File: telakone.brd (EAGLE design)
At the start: 160 x 100 mm, 27 parts, among them X2 MPT0.5/8-2.54

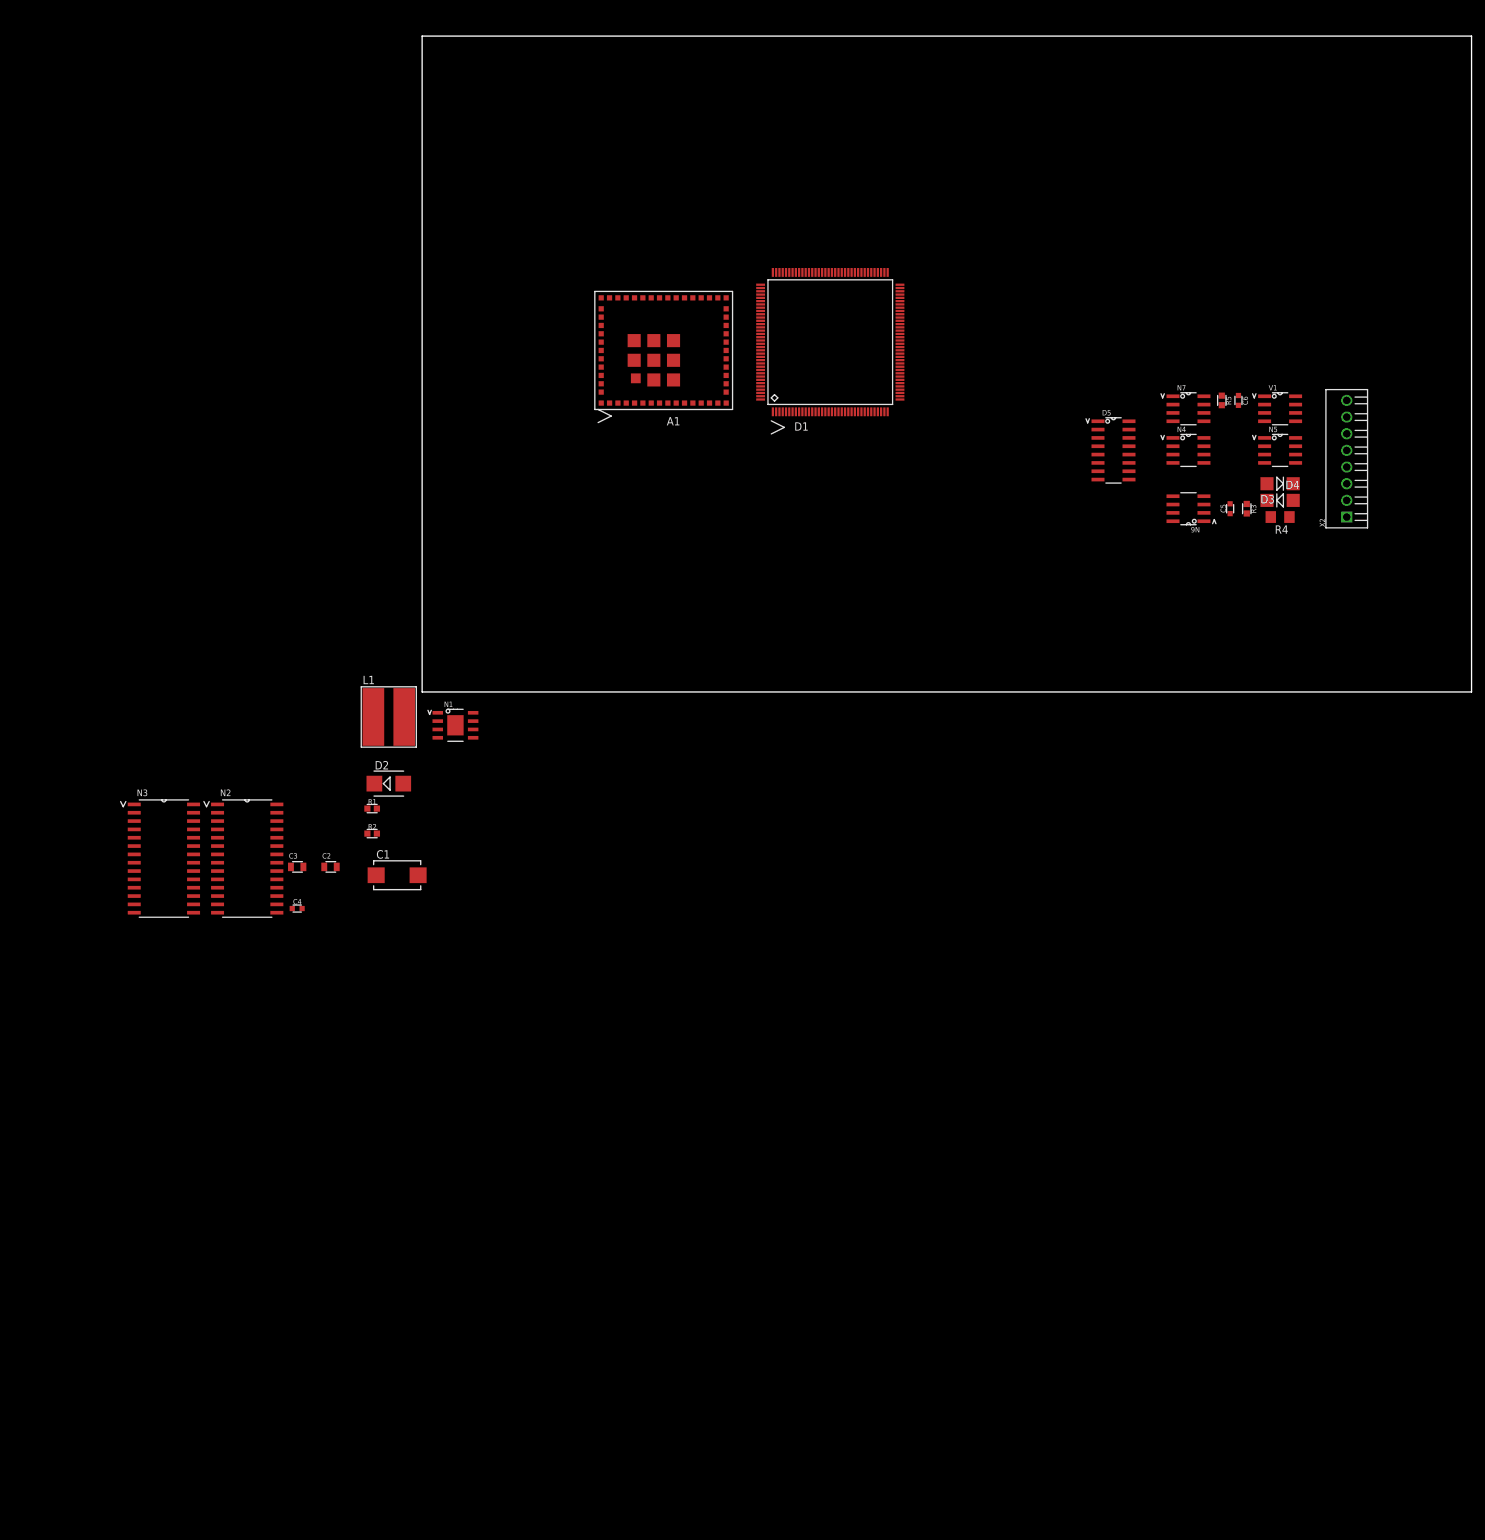
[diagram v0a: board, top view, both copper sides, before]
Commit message: p-fet outputs
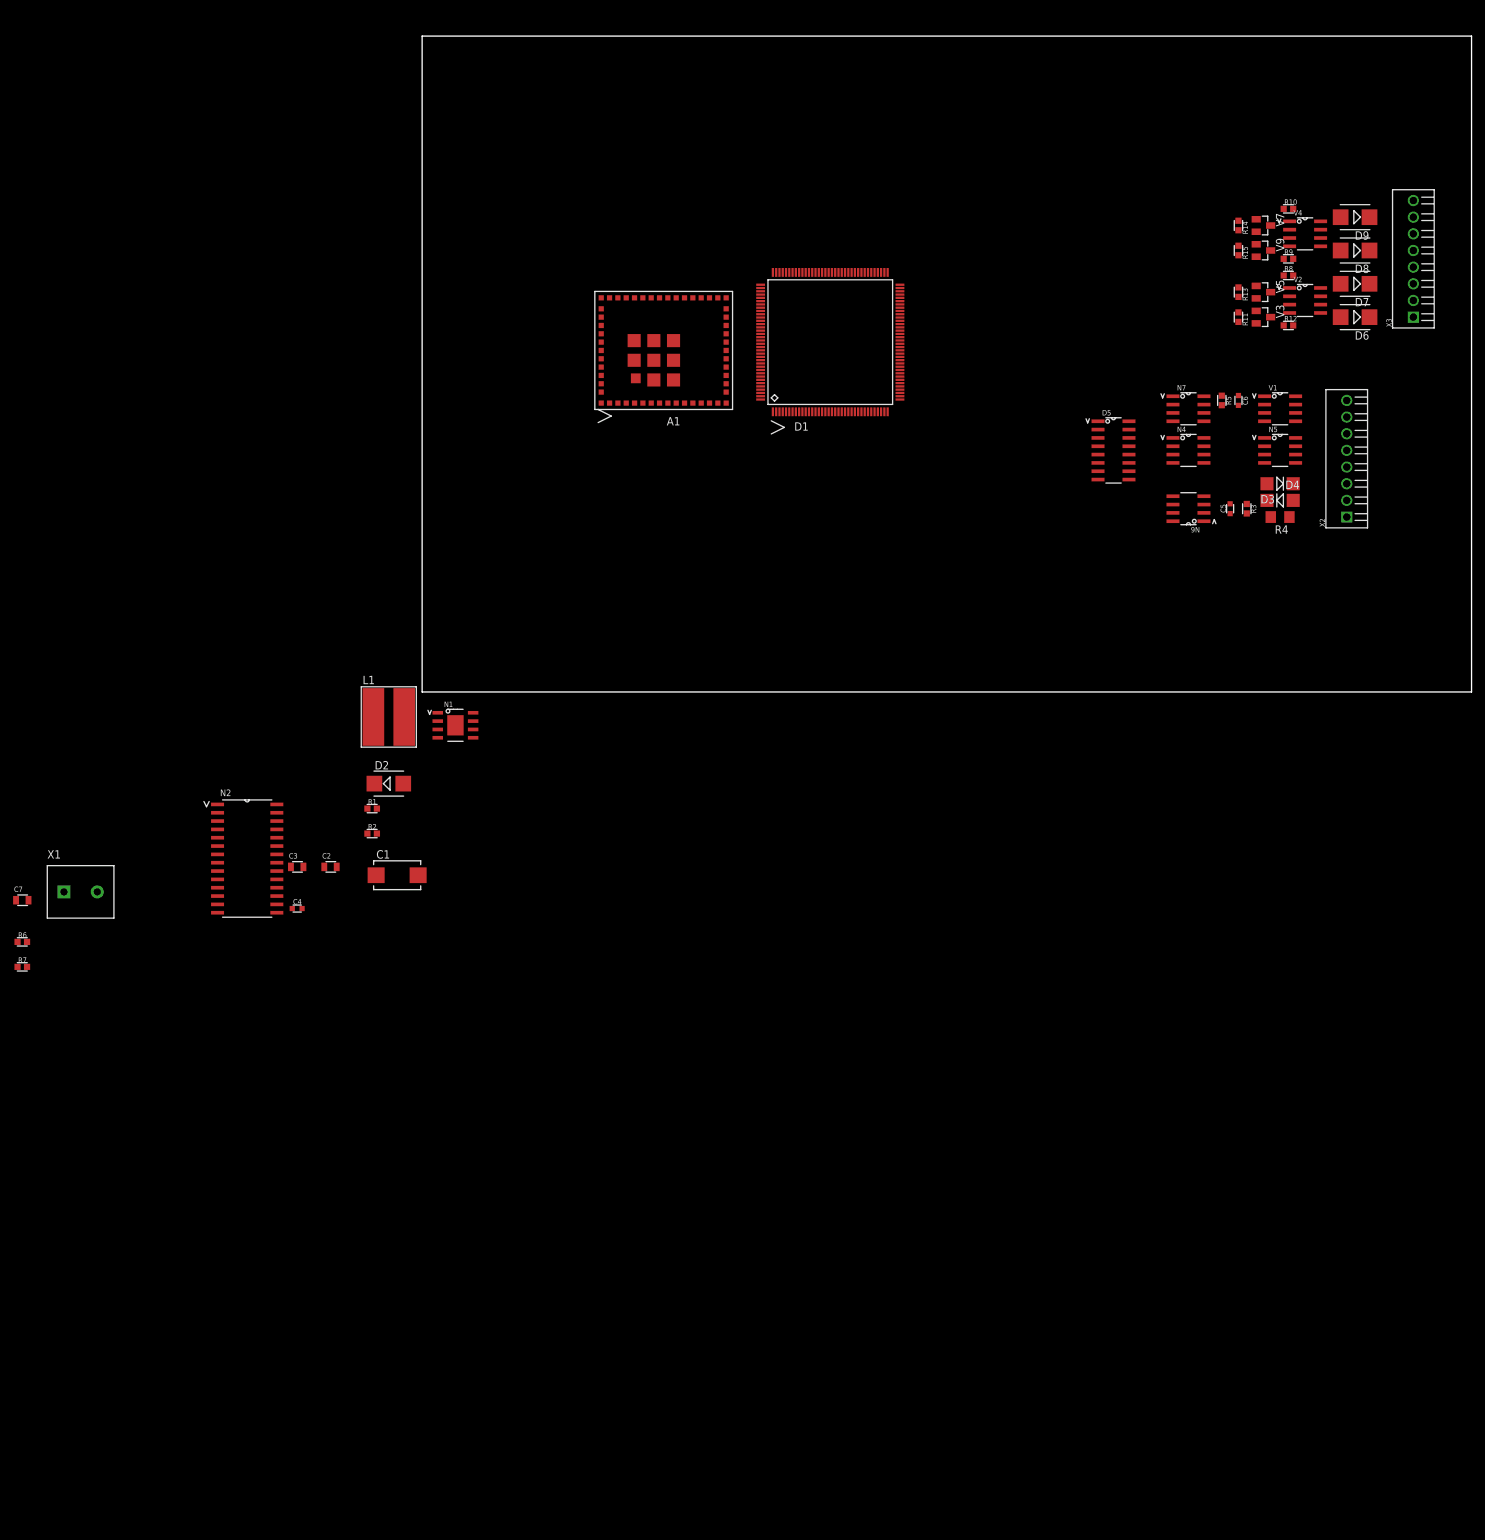
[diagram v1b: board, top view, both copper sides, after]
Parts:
- removed N3: BTM7710G, omat_ic_2:SOIC28-W_MC
- added C7: (no value), omat_ic_2:C0805
- added D6, D7, D8, D9: SK34B, diode:SMB
- added R10, R11, R12, R13, R14, R15, R6, R7, R8, R9: (no value), omat_ic_2:R0603
- added V2, V4: AO4803A, omat_ic_2:SOIC8-N_MC
- added V3, V5, V7, V9: 2N7002K, omat_ic_2:SOT23
- added X1: (no value), omat_ic_2:TE_RUUVILIITIN2
- added X3: MPT0.5/8-2.54, omat_ic_2:MPT0.5/8-2.54
- D2: value STPS340U -> SK34B
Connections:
- new net +12V: C2.1, C3.1, C7.1, N1.7, N2.10, N2.19, N2.24, N2.5, R10.2, R12.2, R8.2, R9.2, V2.1, V2.3, V4.1, V4.3
- new net N$10: R8.1, V2.2, V5.3
- new net N$11: R12.1, V2.4, V3.3
- new net N$12: R13.1, V5.1
- new net N$13: R9.1, V4.4, V7.3
- new net N$14: R14.1, V7.1
- new net N$15: R10.1, V4.2, V9.3
- new net N$16: R15.1, V9.1
- new net N$17: D9.C, X3.7
- new net N$19: D8.C, X3.5
- new net N$20: D7.C, X3.3
- new net N$21: D6.C, X3.1
- new net N$3: N2.12, N2.14, N2.15, N2.18, N2.20, N2.21, X1.1
- new net N$5: N2.1, N2.22, N2.23, N2.25, N2.28, N2.3, X1.2
- new net N$7: N2.8
- new net N$8: N2.13, N2.7, R7.2
- new net N$9: N2.2, N2.9, R6.2
- new net NERT: D6.A, V2.5, V2.6
- new net NERT1: D7.A, V2.7, V2.8
- new net NERT2: D8.A, V4.5, V4.6
- new net NERT3: D9.A, V4.7, V4.8
- net GND: now also C7.2, N2.16, N2.17, N2.26, N2.27, N2.6, R11.2, R13.2, R14.2, R15.2, R6.1, R7.1, V3.2, V5.2, V7.2, V9.2, X3.2, X3.4, X3.6, X3.8
- net N$6: now also R11.1, V3.1; no longer C2.1, C3.1, N1.7

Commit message: placement sketching, temp and acceleration sensors, 2nd drive group
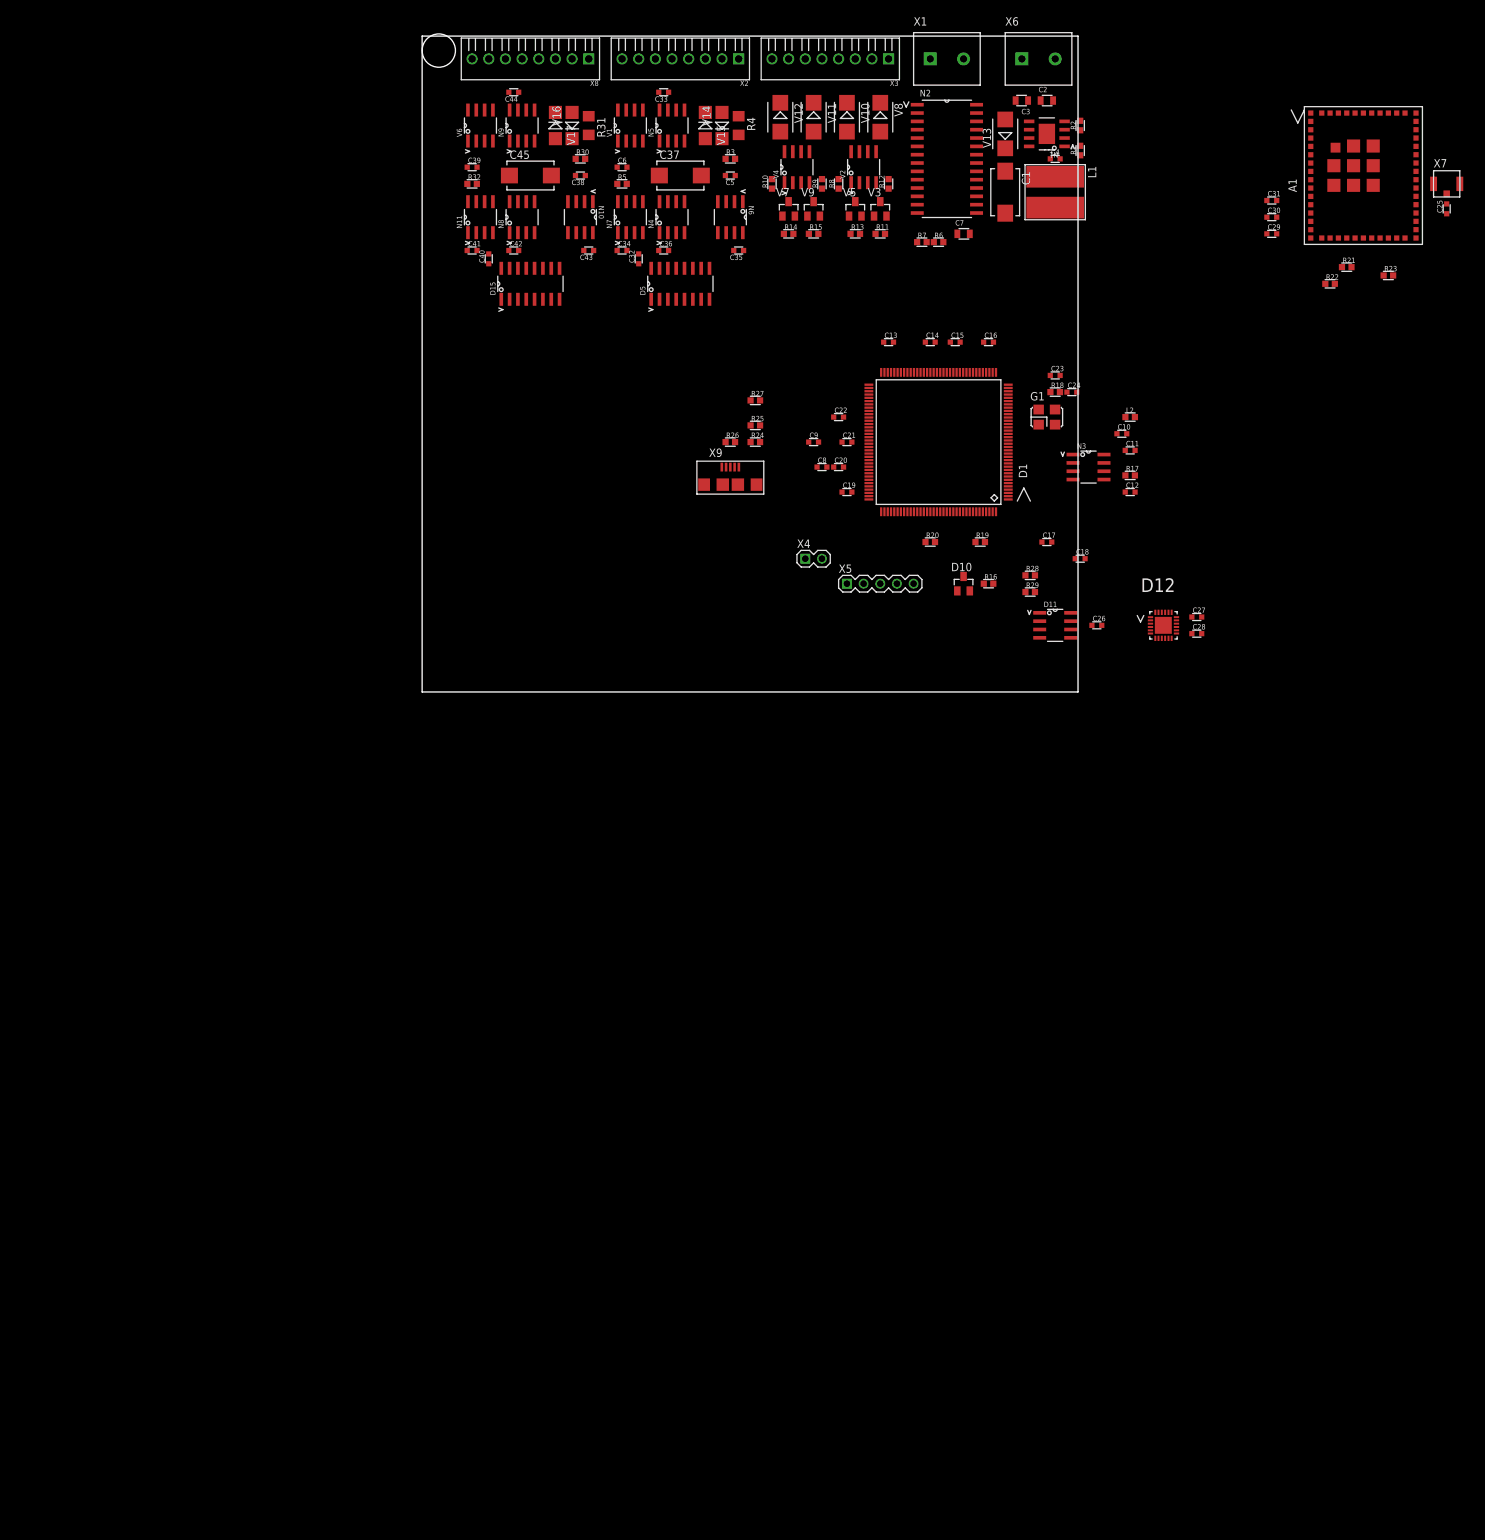
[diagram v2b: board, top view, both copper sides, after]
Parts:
- removed D2, D6, D7, D8, D9: SK34B, diode:SMB
- removed D3, D4: 1SMA5.0AT, EKE:403D-2
- added C10, C11, C12, C13, C14, C15, C16, C17, C18, C19, C20, C21, C22, C23, C24, C26, C27, C28, C29, C30, C31, C32, C33, C34, C35, C36, C38, C39, C40, C41, C42, C43, C44, C8, C9: (no value), omat_ic_2:C0603
- added C25: 10p, omat_ic_2:C0603
- added C37, C45: (no value), EKE:CT7343
- added D10: RT9818C-29GV, omat_ic_2:SOT23
- added D11: LM75BD, omat_ic_2:SOIC8-N_MC
- added D12: IIS328DQTR, omat_ic_2:QFN50P400X400X100-25N
- added D15: SI8661-IS1, omat_ic_2:SOIC16-N
- added G1: 25MHz, omat_ic_2:X_3225
- added L2: IND0603, omat_ic_2:R0603
- added N10: MCP3201/SN, omat_ic_2:SOIC8-N_MC
- added N11, N3: MCP1501/SN, omat_ic_2:SOIC8-N_MC
- added N8: MCP4921/SN, omat_ic_2:SOIC8-N_MC
- added N9: TS921IDT, omat_ic_2:SOIC8-N_MC
- added R16, R17, R18, R19, R20, R21, R22, R23, R27, R28, R29, R32: (no value), omat_ic_2:R0603
- added R24, R25: 22, omat_ic_2:R0603
- added R26: 1k, omat_ic_2:R0603
- added R30: 825, omat_ic_2:R0603
- added R31: 19k1, omat_ic_2:R1206
- added V10, V11, V12, V13, V8: SK34B, diode:SMB
- added V14, V15, V16, V17: 1SMA5.0AT, EKE:403D-2
- added V6: AO4886, omat_ic_2:SOIC8-N_MC
- added X4: PIIKKIRIMA-2, omat_ic_2:PIIKKIRIMA-2
- added X5: PIIKKIRIMA-5, omat_ic_2:PIIKKIRIMA-5
- added X6: (no value), omat_ic_2:TE_RUUVILIITIN2
- added X7: U.FL-R-SMT-1, omat_ic_2:U.FL-R-SMT-1
- added X8: MPT0.5/8-2.54, omat_ic_2:MPT0.5/8-2.54
- added X9: 629105136821, omat_ic_2:629105136821
- moved X1 183.2 mm to (77.5, 96.5)
- moved R7 176.1 mm to (76.2, 68.6)
- moved C7 175.8 mm to (82.5, 69.8)
- moved R6 175.8 mm to (78.7, 68.6)
- moved C4 162.5 mm to (96.5, 81.3)
- moved C3 160.8 mm to (91.4, 90.2), turned to 180 degrees
- moved C2 159.9 mm to (95.2, 90.2)
- moved R2 152.7 mm to (100.3, 86.4), turned to 90 degrees
- moved N2 150.9 mm to (80.0, 81.3)
- moved R1 147.4 mm to (100.3, 82.5), turned to 90 degrees
- moved C1 139.4 mm to (88.9, 76.2), turned to 270 degrees
- moved L1 129.3 mm to (96.5, 76.2), turned to 270 degrees
- moved N1 127.5 mm to (95.2, 85.1), turned to 180 degrees
- moved X2 116.1 mm to (48.3, 96.5), turned to 180 degrees
- moved A1 110.0 mm to (143.5, 78.7), turned to 90 degrees
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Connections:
- net +48V renamed +48V_1
- net BRAKE renamed BRAKE_1
- net BRAKE_OD renamed BRAKE_OD_1
- net REVERSE renamed REVERSE_1
- net REVERSE_OD renamed REVERSE_OD_1
- net SPICLK renamed SPICLK_1
- net SPICSL renamed SPICSL_1
- net SPIMISO renamed SPIMISO_1
- net SPIMOSI renamed SPIMOSI_1
- net THROTTLE renamed THROTTLE_1
- net THROTTLE_BUFFERED renamed THROTTLE_BUFFERED_1
- net VREF+2V5 renamed VREF25_1
- removed net AIN: C5.1, D4.P$2, N6.2, R3.2, R4.2
- removed net V+: D3.P$2, D5.16, N4.1, N5.7, N6.8, N7.1, N7.3, X2.4
- removed net V-: C5.2, C6.2, D3.P$1, D4.P$1, D5.9, N4.5, N4.7, N5.4, N6.3, N6.4, N7.2, N7.4, N7.5, N7.6, R3.1, V1.1, V1.3, X2.3, X2.8
- new net +48V_2: R31.1, X8.1, X8.2
- new net AIN_1: C5.1, N6.2, R3.2, R4.2, V14.P$2
- new net AIN_2: C38.1, N10.2, R30.2, R31.2, V16.P$2
- new net BOOT0: D1.138, R19.2, X4.2
- new net BRAKE_2: D15.12, V6.4
- new net BRAKE_OD_2: V6.5, V6.6, X8.6
- new net CCHIBL: A1.P4, D1.36
- new net CCIRQ: A1.P11, D1.40
- new net CCSPICLK: A1.P5, D1.41
- new net CCSPICSL: A1.P8, D1.37
- new net CCSPIMISO: A1.P7, D1.42
- new net CCSPIMOSI: A1.P6, D1.43
- new net I2CSCL: D1.136, D11.2, D12.11, R29.1
- new net I2CSDA: D1.137, D11.1, D12.16, R28.1
- new net N$22: C8.1, D1.106
- new net N$23: C9.1, D1.71
- new net N$24: C12.1, R17.1
- new net N$25: C10.1, C11.1, D1.33, L2.1
- new net N$26: C23.1, D1.23, G1.1
- new net N$27: D1.24, R18.2
- new net N$28: C24.1, G1.3, R18.1
- new net N$29: D1.48, R20.2
- new net N$30: A1.P31, C25.1
- new net N$31: C25.2, X7.SIG
- new net N$32: A1.P21, R21.2
- new net N$33: D1.103, R24.2
- new net N$34: A1.P10, R22.2
- new net N$35: A1.P23, R23.2
- new net N$36: D1.104, R25.2
- new net N$37: R25.1, X9.3
- new net N$38: R24.1, X9.2
- new net N$39: D1.101, R26.2
- new net N$40: R26.1, X9.1
- new net N$41: D1.102, R27.2
- new net N$42: C39.1, R32.1
- new net RESETL: A1.P35, D1.25, D10.1, R16.1, X5.4
- new net REVERSE_2: D15.11, V6.2
- new net REVERSE_OD_2: V6.7, V6.8, X8.7
- new net SPICLK_2: D15.14, N10.7, N8.3
- new net SPICSL_2: D15.15, N10.5, N8.2
- new net SPIMISO_2: D15.10, N10.6
- new net SPIMOSI_2: D15.13, N8.4
- new net SWCLK: D1.109, X5.3
- new net SWDIO: D1.105, X5.2
- new net THROTTLE_2: N8.8, N9.3
- new net THROTTLE_BUFFERED_2: N9.2, N9.6, X8.5
- new net V+1: C32.1, C33.1, C34.1, C35.1, C36.1, C37.+, D5.16, N4.1, N5.7, N6.8, N7.1, N7.3, V15.P$2, X2.4
- new net V+2: C40.1, C41.1, C42.1, C43.1, C44.1, C45.+, D15.16, N10.8, N11.1, N11.3, N8.1, N9.7, V17.P$2, X8.4
- new net V-1: C32.2, C33.2, C34.2, C35.2, C36.2, C37.-, C5.2, C6.2, D5.9, N4.5, N4.7, N5.4, N6.3, N6.4, N7.2, N7.4, N7.5, N7.6, R3.1, V1.1, V1.3, V14.P$1, V15.P$1, X2.3, X2.8
- new net V-2: C38.2, C39.2, C40.2, C41.2, C42.2, C43.2, C44.2, C45.-, D15.9, N10.3, N10.4, N11.2, N11.4, N11.5, N11.6, N8.5, N8.7, N9.4, R30.1, V16.P$1, V17.P$1, V6.1, V6.3, X8.3, X8.8
- new net VREF25: D1.32, N3.7, N3.8, R17.2
- new net VREF25_2: N10.1, N11.7, N11.8, N8.6, R32.2
- net +12V: now also X6.1
- net +3V3: now also A1.P36, A1.P37, A1.P40, C13.1, C14.1, C15.1, C16.1, C17.1, C18.1, C19.1, C20.1, C21.1, C22.1, C26.1, C27.1, C28.1, C29.1, C30.1, C31.1, D1.108, D1.121, D1.131, D1.143, D1.144, D1.17, D1.30, D1.39, D1.52, D1.6, D1.62, D1.72, D1.84, D1.95, D10.3, D11.8, D12.12, D12.13, D12.14, D12.5, D15.1, L2.2, N3.1, N3.3, R16.2, R27.1, R28.2, R29.2, X4.1, X5.1
- net GND: now also A1.P1, A1.P16, A1.P2, A1.P27, A1.P28, A1.P30, A1.P32, A1.P38, A1.P43, A1.P55, A1.P56, A1.P57, A1.P58, A1.P59, A1.P60, A1.P61, A1.P62, A1.P63, C10.2, C11.2, C12.2, C13.2, C14.2, C15.2, C16.2, C17.2, C18.2, C19.2, C20.2, C21.2, C22.2, C23.2, C24.2, C26.2, C27.2, C28.2, C29.2, C30.2, C31.2, C8.2, C9.2, D1.107, D1.120, D1.130, D1.16, D1.31, D1.38, D1.51, D1.61, D1.83, D1.94, D10.2, D11.4, D11.5, D11.6, D11.7, D12.10, D12.15, D12.25, D12.4, D12.6, D12.8, D12.9, D15.8, N3.2, N3.4, N3.5, N3.6, R19.1, R20.1, R21.1, R22.1, R23.1, V13.A, X5.5, X6.2, X7.GND1, X7.GND2, X9.5, X9.Z1, X9.Z2, X9.Z3, X9.Z4; no longer D2.A
- net N$1: now also V13.C; no longer D2.C
- net N$17: now also V12.C; no longer D9.C
- net N$19: now also V11.C; no longer D8.C
- net N$20: now also V10.C; no longer D7.C
- net N$21: now also V8.C; no longer D6.C
- net NERT: now also V8.A; no longer D6.A
- net NERT1: now also V10.A; no longer D7.A
- net NERT2: now also V11.A; no longer D8.A
- net NERT3: now also V12.A; no longer D9.A
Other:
- board size 160 x 100 mm -> 100 x 100 mm
